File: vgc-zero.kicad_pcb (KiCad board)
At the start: 2 copper layers, 50 x 90 mm, 26 parts, among them J1 Conn_01x06_Pin, J2 Conn_01x06_Pin, J3 Conn_01x06_Pin, SW1 SW_Push, SW10 SW_Push, SW11 SW_SPDT, SW2 SW_Push, SW3 SW_Push, SW4 SW_Push, SW5 SW_Push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

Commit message: bump version
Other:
- board text added: "vgc zero v1.1.1"
- board text removed: "vgc zero v1.1.0"
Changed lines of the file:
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@@
 	(title_block
 		(title "vgc zero")
-		(rev "v1.1.0")
+		(rev "v1.1.1")
 		(comment 3 "Company: chilichip")
 		(comment 4 "Author: Kacper Akdag-Ochnik")
@@
 		(layer "User.1")
 	)
-	(gr_text "vgc zero v1.1.0"
+	(gr_text "vgc zero v1.1.1"
 		(at 56.32 122.82 0)
 		(layer "F.SilkS")

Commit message: major improvements
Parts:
- removed H1, H2, H3, H4: MountingHole_Pad, MountingHole:MountingHole_2.2mm_M2_Pad
- removed LS1: Speaker, Buzzer_Beeper:Buzzer_12x9.5RM7.6
- removed OLED1: DISP1, Connector_JST:JST_PH_S7B-PH-K_1x07_P2.00mm_Horizontal
- added Buzz1: Buzzer, Buzzer_Beeper:Buzzer_12x9.5RM7.6, B.Cu at (97.5, 56.2)
- added DISP1: DISPLAY, vgc-zero-footprints:SSD1351_OLED_128x128_WAVESHARE, F.Cu at (57.2, 41.5)
- added DISP1_CONN1: DISPLAY_CONNECTOR, Connector_JST:JST_PH_S7B-PH-K_1x07_P2.00mm_Horizontal, B.Cu at (63.7, 66.0)
- added REF**: MountingHole_2.2mm_M2, MountingHole:MountingHole_2.2mm_M2, F.Cu at (102.5, 40.0)
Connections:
- MCU1 pad 22: Net-(MCU1-GPIO17) -> /DISP_CS
- MCU1 pad 24: Net-(MCU1-GPIO18) -> /DISP_CLK
- MCU1 pad 25: Net-(MCU1-GPIO19) -> /DISP_DIN
- MCU1 pad 26: Net-(MCU1-GPIO20) -> /DISP_RST
- MCU1 pad 27: Net-(MCU1-GPIO21) -> /DISP_DC
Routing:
- net /DISP_CS: track 0.00 -> 40.0 mm
- net Net-(MCU1-GPIO17): track 33.0 -> 0.00 mm
- net Net-(MCU1-GPIO20): track 27.4 -> 0.00 mm, vias 1 -> 0
- net /DISP_RST: track 0.00 -> 27.4 mm, vias 0 -> 1
- net /DISP_CLK: track 0.00 -> 25.1 mm
- net Net-(MCU1-GPIO18): track 25.0 -> 0.00 mm
- net Net-(MCU1-GPIO21): track 23.1 -> 0.00 mm, vias 1 -> 0
- net /DISP_DC: track 0.00 -> 23.1 mm, vias 0 -> 1
- net /DISP_DIN: track 0.00 -> 20.0 mm
- net Net-(MCU1-GPIO19): track 19.8 -> 0.00 mm
- net Net-(J2-Pin_3): track 112.4 -> 108.6 mm
- net Net-(MCU1-GPIO16): track 60.4 -> 61.3 mm
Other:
- outline, holes or cut-outs redrawn
- board text added: "H1"
- board text added: "H2"
- board text added: "H3"
- board text added: "H4"
- board text added: "Made by teriyaki"
- board text added: "vgc zero v1.1.2"
- board text removed: "vgc zero v1.1.1"

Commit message: minor improvements
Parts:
- R1: moved to B.Cu
- moved D1 16.4 mm to (79.5, 39.8)
- moved R1 0.05 mm to (60.2, 39.7)
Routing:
- net Net-(D1-A): track 30.2 -> 13.8 mm
- net Net-(Buzz1-+): track 43.6 -> 33.8 mm, vias 1 -> 0
- net Net-(J2-Pin_4): track 88.2 -> 81.1 mm
- net /DISP_DC: track 23.1 -> 24.6 mm
- net /DISP_RST: track 27.4 -> 28.8 mm
- net /DISP_DIN: track 20.0 -> 21.0 mm
- net /DISP_CS: track 40.0 -> 39.5 mm
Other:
- board text added: "vgc zero v1.1.3"
- board text removed: "vgc zero v1.1.2"

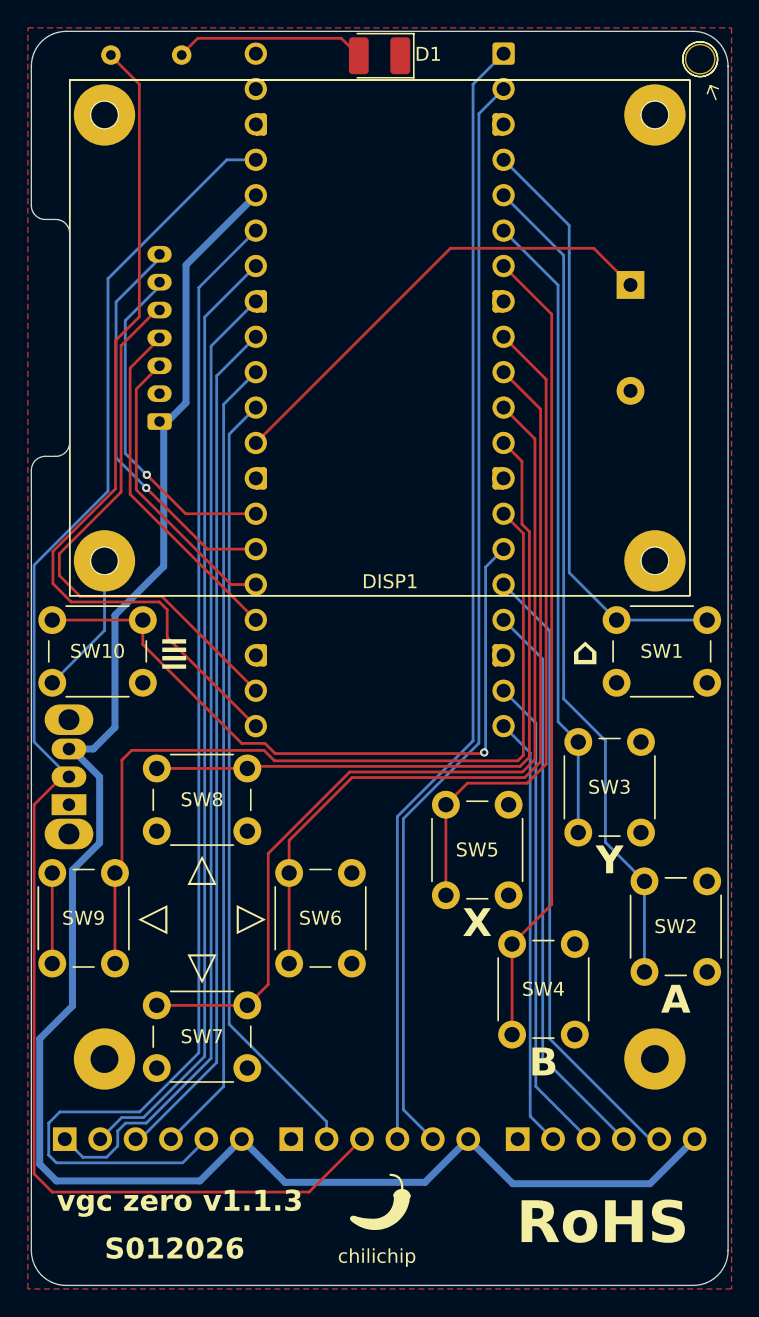
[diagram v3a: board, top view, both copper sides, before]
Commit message: fix overlap
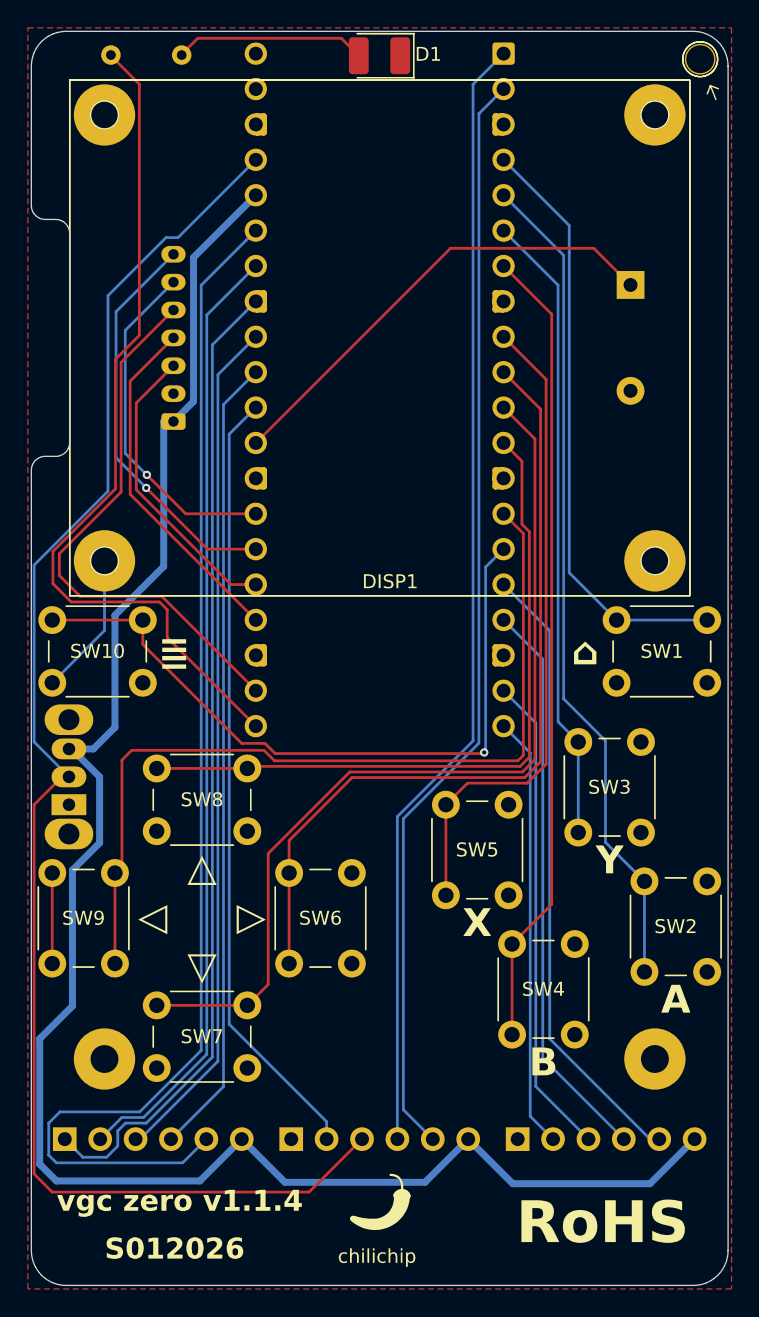
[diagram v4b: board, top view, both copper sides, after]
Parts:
- moved DISP1_CONN1 1.00 mm to (64.7, 66.0)
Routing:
- net Net-(J2-Pin_3): track 108.6 -> 107.9 mm
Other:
- board text added: "vgc zero v1.1.4"
- board text removed: "vgc zero v1.1.3"
